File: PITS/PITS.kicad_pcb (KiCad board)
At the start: 2 copper layers, 65 x 30 mm, 56 parts, among them P1 CONN_02X20, P10 I2C, P11 I2C, P12 I2C, P13 I2C, P14 BATT, P2 BNC, P3 BNC, P4 BNC, P5 BNC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

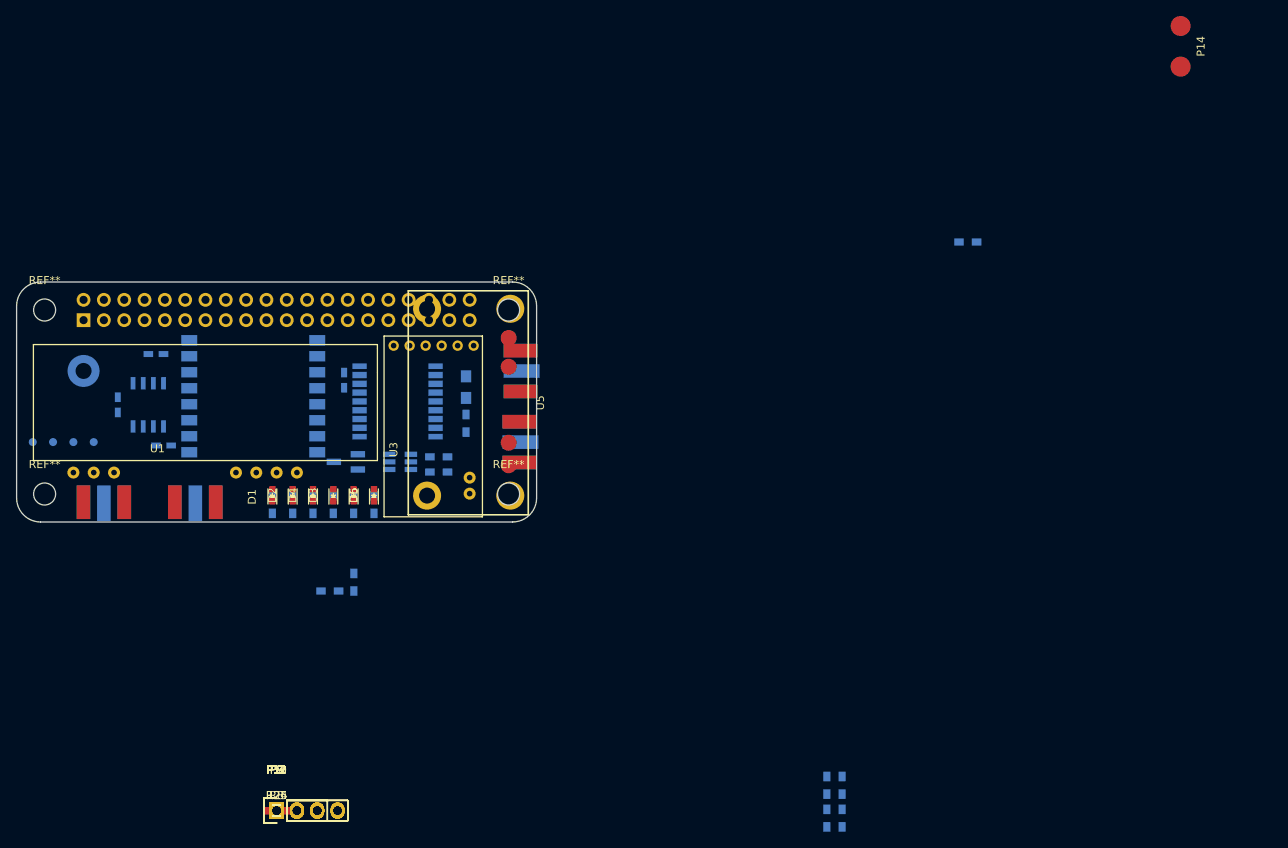
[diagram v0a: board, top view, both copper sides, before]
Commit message: layout - work in progress - first placement
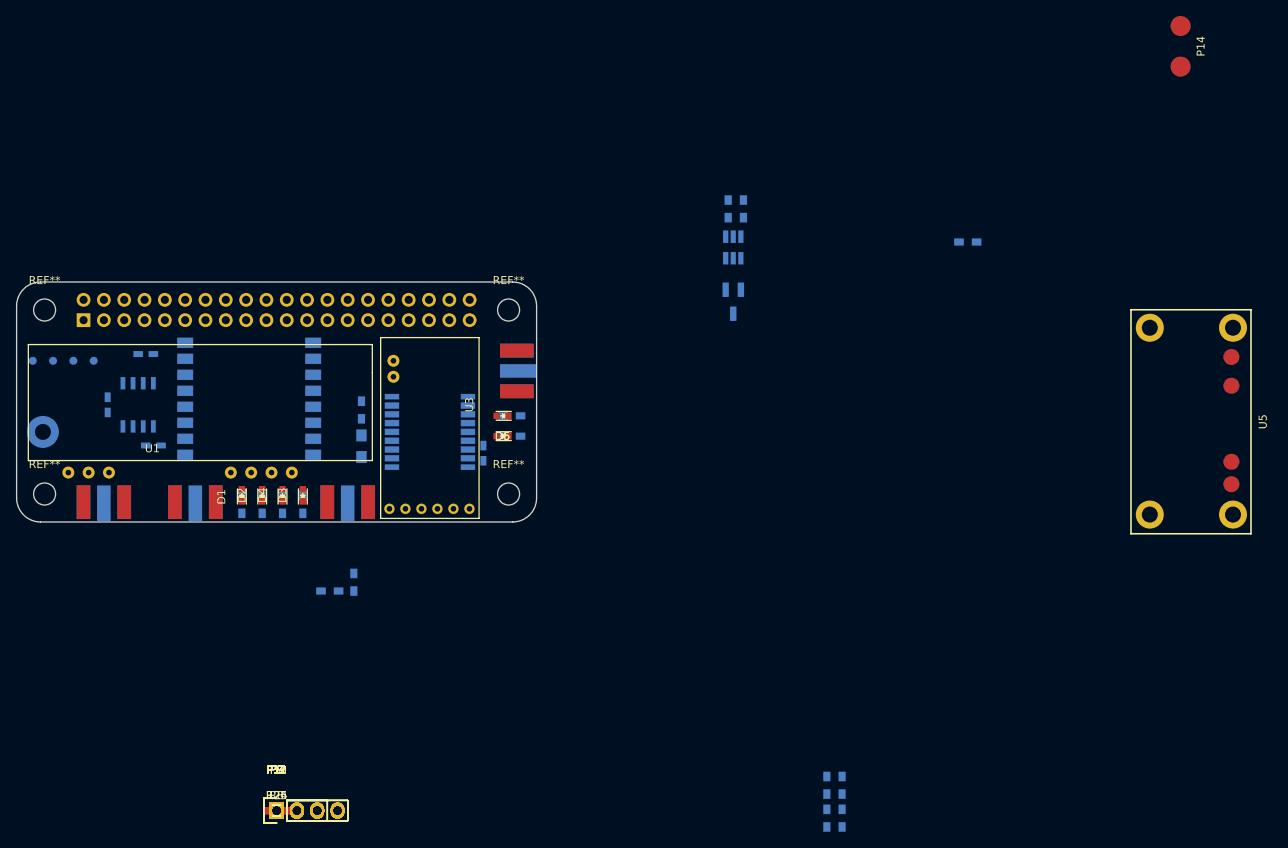
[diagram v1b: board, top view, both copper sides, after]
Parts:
- moved U5 90.4 mm to (201.8, 66.5)
- moved Q1 52.4 mm to (144.6, 51.5), turned to 0 degrees
- moved R19 50.3 mm to (145.9, 39.9), turned to 90 degrees
- moved Q2 49.5 mm to (144.6, 44.7), turned to 270 degrees
- moved R6 47.6 mm to (143.9, 39.9), turned to 90 degrees
- moved P2 27.3 mm to (96.4, 76.6), turned to 90 degrees
- moved R22 21.5 mm to (116.9, 68.3), turned to 180 degrees
- moved U3 20.5 mm to (101.6, 58.4), turned to 270 degrees
- moved R23 20.5 mm to (116.9, 65.7), turned to 180 degrees
- moved D5 20.0 mm to (115.7, 68.3), turned to 180 degrees
- moved C14 19.7 mm to (113.3, 70.4), turned to 90 degrees
- moved D6 18.9 mm to (115.7, 65.7), turned to 180 degrees
- moved L1 15.0 mm to (98.1, 69.5), turned to 90 degrees
- moved U2 14.4 mm to (111.4, 63.3), turned to 0 degrees
- moved R1 13.2 mm to (98.1, 65.0), turned to 270 degrees
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
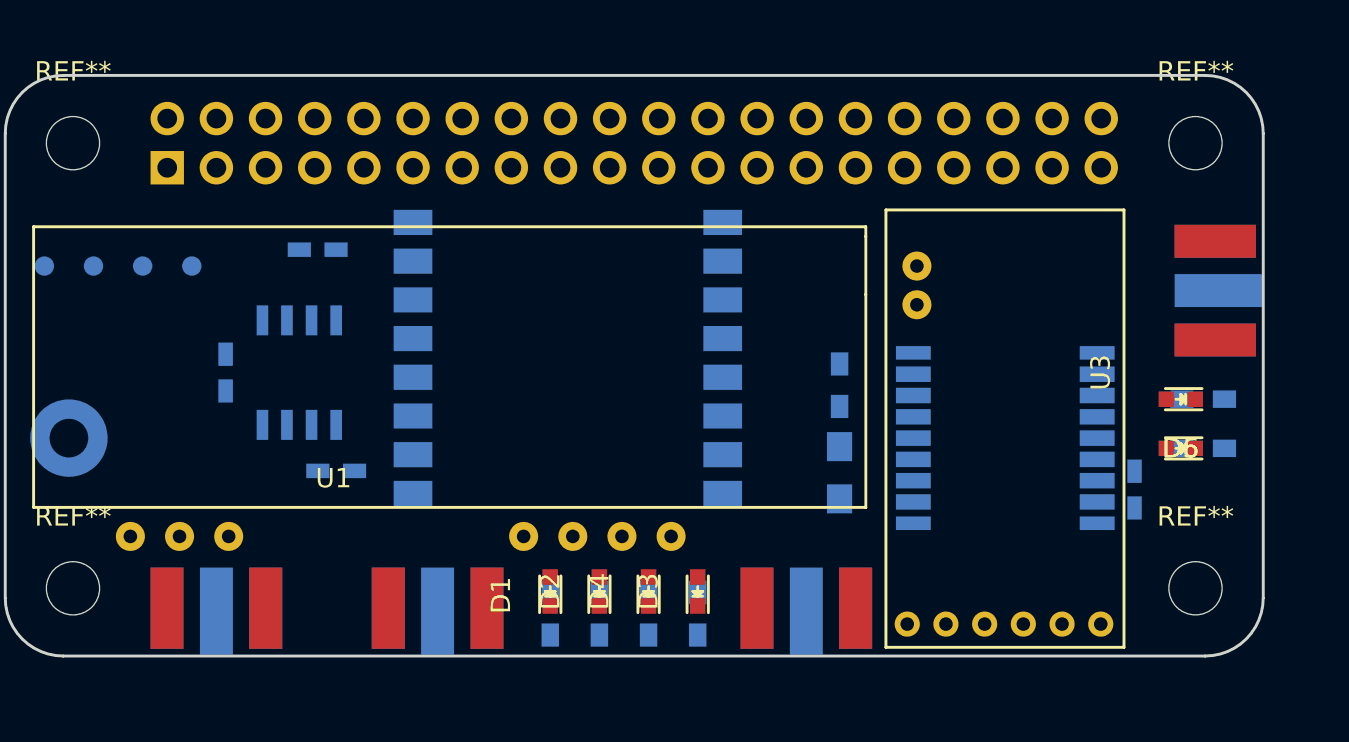
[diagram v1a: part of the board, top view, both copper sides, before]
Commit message: layout - work in progress - first placement
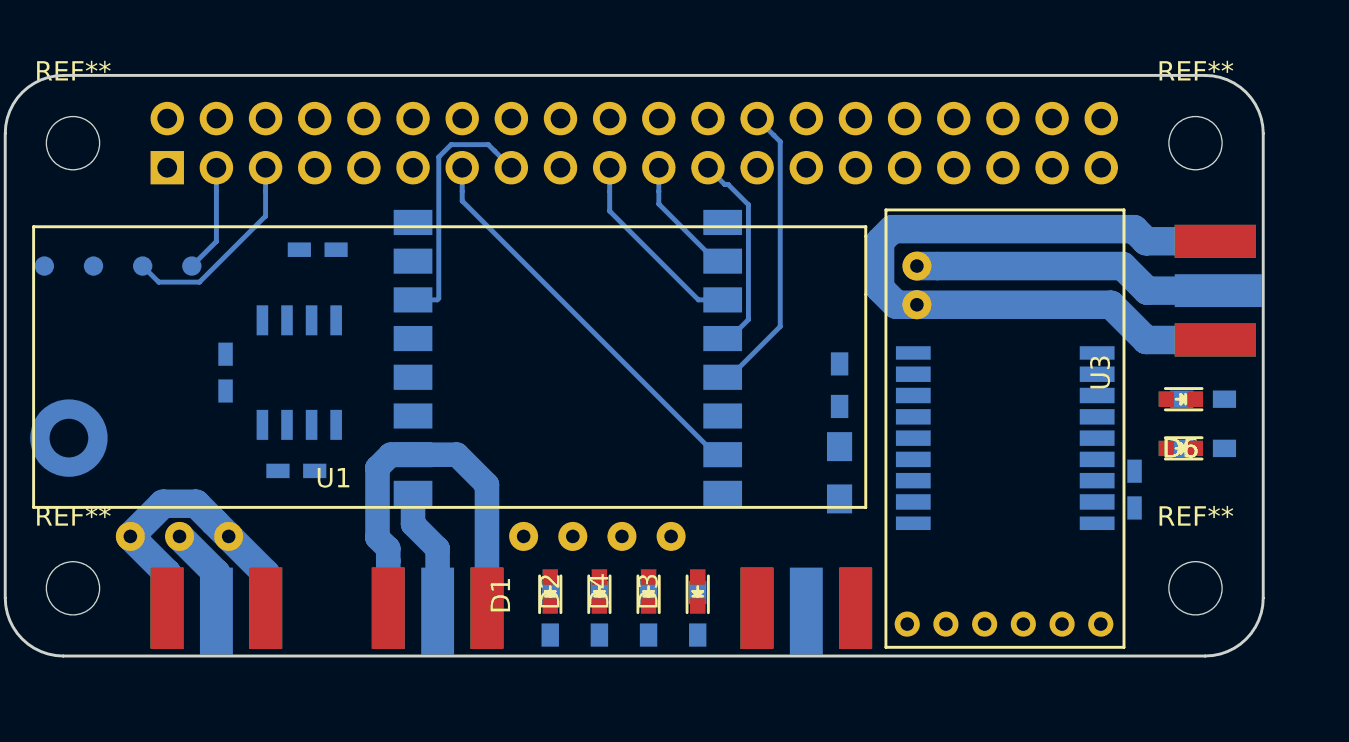
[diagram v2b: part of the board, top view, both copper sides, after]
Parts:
- moved C2 2.06 mm to (70.0, 69.4)
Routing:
- net GND: track 0.00 -> 74.6 mm
- net /GPIO27: track 0.00 -> 20.6 mm
- net Net-(P4-Pad1): track 0.00 -> 16.1 mm
- net /GPIO7(CE1): track 0.00 -> 15.3 mm
- net /GPIO22: track 0.00 -> 13.2 mm
- net /GPIO3(SCL1): track 0.00 -> 10.6 mm
- net /GPIO11(SCLK0): track 0.00 -> 10.6 mm
- net /GPIO10(MOSI0): track 0.00 -> 9.98 mm
- net Net-(P5-Pad1): track 0.00 -> 6.61 mm
- net /GPIO9(MISO0): track 0.00 -> 6.40 mm
- net /GPIO2(SDA1): track 0.00 -> 5.61 mm
- net Net-(P3-Pad1): track 0.00 -> 4.65 mm
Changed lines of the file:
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@@
     (thickness 1.6)
     (drawings 10)
-    (tracks 0)
+    (tracks 74)
     (zones 0)
     (modules 56)
@@
   )
   (setup
-    (last_trace_width 0.9144)
+    (last_trace_width 0.254)
     (user_trace_width 0.4064)
     (user_trace_width 0.9144)
@@
   )
   (module Capacitors_SMD:C_0603_HandSoldering (layer B.Cu)
-    (at 72.1 69.435 180)
+    (at 70.04 69.435 180)
     (descr "Capacitor SMD 0603, hand soldering")
     (tags "capacitor 0603")
@@
   (gr_arc (start 58 52) (end 55 52) (angle 90) (layer Edge.Cuts) (width 0.15))
   (gr_line (start 58 79) (end 117 79) (angle 90) (layer Edge.Cuts) (width 0.15))
+  (segment (start 65.91 54.991314) (end 65.91 53.77) (width 0.254) (layer B.Cu) (net 3))
+  (segment (start 65.91 57.58) (end 65.91 54.991314) (width 0.254) (layer B.Cu) (net 3))
+  (segment (start 64.64 58.85) (end 65.91 57.58) (width 0.254) (layer B.Cu) (net 3))
+  (segment (start 65.038497 59.680201) (end 68.45 56.268698) (width 0.254) (layer B.Cu) (net 4))
+  (segment (start 62.930201 59.680201) (end 65.038497 59.680201) (width 0.254) (layer B.Cu) (net 4))
+  (segment (start 68.45 54.991314) (end 68.45 53.77) (width 0.254) (layer B.Cu) (net 4))
+  (segment (start 62.1 58.85) (end 62.930201 59.680201) (width 0.254) (layer B.Cu) (net 4))
+  (segment (start 68.45 56.268698) (end 68.45 54.991314) (width 0.254) (layer B.Cu) (net 4))
+  (segment (start 117.5244 57.57) (end 113.9512 57.57) (width 1.4732) (layer B.Cu) (net 5))
+  (segment (start 113.9512 57.57) (end 113.3262 56.945) (width 1.4732) (layer B.Cu) (net 5))
+  (segment (start 113.3262 56.945) (end 100.835 56.945) (width 1.4732) (layer B.Cu) (net 5))
+  (segment (start 100.835 56.945) (end 100.2 57.58) (width 1.4732) (layer B.Cu) (net 5))
+  (segment (start 100.2 57.58) (end 100.2 60.00566) (width 1.4732) (layer B.Cu) (net 5))
+  (segment (start 100.2 60.00566) (end 101.04434 60.85) (width 1.4732) (layer B.Cu) (net 5))
+  (segment (start 101.04434 60.85) (end 102.105 60.85) (width 1.4732) (layer B.Cu) (net 5))
+  (segment (start 102.105 60.85) (end 112.1312 60.85) (width 1.4732) (layer B.Cu) (net 5))
+  (segment (start 117.5244 62.67) (end 113.9512 62.67) (width 1.4732) (layer B.Cu) (net 5))
+  (segment (start 113.9512 62.67) (end 112.1312 60.85) (width 1.4732) (layer B.Cu) (net 5))
+  (segment (start 76.07 68.5975) (end 74.911238 68.5975) (width 1.27) (layer B.Cu) (net 5))
+  (segment (start 74.911238 68.5975) (end 74.231799 69.276939) (width 1.27) (layer B.Cu) (net 5))
+  (segment (start 74.231799 69.276939) (end 74.231799 72.886799) (width 1.27) (layer B.Cu) (net 5))
+  (segment (start 74.79 73.445) (end 74.79 74.08) (width 1.27) (layer B.Cu) (net 5))
+  (segment (start 74.231799 72.886799) (end 74.79 73.445) (width 1.27) (layer B.Cu) (net 5))
+  (segment (start 74.79 74.08) (end 74.79 76.53) (width 1.27) (layer B.Cu) (net 5))
+  (segment (start 79.89 76.53) (end 79.89 70.1475) (width 1.27) (layer B.Cu) (net 5))
+  (segment (start 79.89 70.1475) (end 78.34 68.5975) (width 1.27) (layer B.Cu) (net 5))
+  (segment (start 78.34 68.5975) (end 76.07 68.5975) (width 1.27) (layer B.Cu) (net 5))
+  (segment (start 61.465 72.82) (end 63.154801 71.130199) (width 1.4732) (layer B.Cu) (net 5))
+  (segment (start 63.154801 71.130199) (end 64.855199 71.130199) (width 1.4732) (layer B.Cu) (net 5))
+  (segment (start 64.855199 71.130199) (end 65.795001 72.070001) (width 1.4732) (layer B.Cu) (net 5))
+  (segment (start 65.795001 72.070001) (end 66.545 72.82) (width 1.4732) (layer B.Cu) (net 5))
+  (segment (start 63.36 76.53) (end 63.36 74.715) (width 1.4732) (layer B.Cu) (net 5))
+  (segment (start 63.36 74.715) (end 61.465 72.82) (width 1.4732) (layer B.Cu) (net 5))
+  (segment (start 68.46 76.53) (end 68.46 74.735) (width 1.4732) (layer B.Cu) (net 5))
+  (segment (start 68.46 74.735) (end 66.545 72.82) (width 1.4732) (layer B.Cu) (net 5))
+  (segment (start 92.07 68.5975) (end 91.72 68.5975) (width 0.254) (layer B.Cu) (net 11))
+  (segment (start 91.72 68.5975) (end 78.61 55.4875) (width 0.254) (layer B.Cu) (net 11))
+  (segment (start 78.61 55.4875) (end 78.61 54.991314) (width 0.254) (layer B.Cu) (net 11))
+  (segment (start 78.61 54.991314) (end 78.61 53.77) (width 0.254) (layer B.Cu) (net 11))
+  (segment (start 76.07 60.5975) (end 77.324 60.5975) (width 0.254) (layer B.Cu) (net 12))
+  (segment (start 77.400201 60.521299) (end 77.400201 53.212973) (width 0.254) (layer B.Cu) (net 12))
+  (segment (start 77.324 60.5975) (end 77.400201 60.521299) (width 0.254) (layer B.Cu) (net 12))
+  (segment (start 77.400201 53.212973) (end 78.036975 52.576199) (width 0.254) (layer B.Cu) (net 12))
+  (segment (start 78.036975 52.576199) (end 79.956199 52.576199) (width 0.254) (layer B.Cu) (net 12))
+  (segment (start 79.956199 52.576199) (end 80.286401 52.906401) (width 0.254) (layer B.Cu) (net 12))
+  (segment (start 80.286401 52.906401) (end 81.15 53.77) (width 0.254) (layer B.Cu) (net 12))
+  (segment (start 92.07 60.5975) (end 90.816 60.5975) (width 0.254) (layer B.Cu) (net 13))
+  (segment (start 90.816 60.5975) (end 86.23 56.0115) (width 0.254) (layer B.Cu) (net 13))
+  (segment (start 86.23 54.991314) (end 86.23 53.77) (width 0.254) (layer B.Cu) (net 13))
+  (segment (start 86.23 56.0115) (end 86.23 54.991314) (width 0.254) (layer B.Cu) (net 13))
+  (segment (start 92.07 58.5975) (end 91.72 58.5975) (width 0.254) (layer B.Cu) (net 14))
+  (segment (start 91.72 58.5975) (end 88.77 55.6475) (width 0.254) (layer B.Cu) (net 14))
+  (segment (start 88.77 55.6475) (end 88.77 54.991314) (width 0.254) (layer B.Cu) (net 14))
+  (segment (start 88.77 54.991314) (end 88.77 53.77) (width 0.254) (layer B.Cu) (net 14))
+  (segment (start 92.07 62.5975) (end 92.42 62.5975) (width 0.254) (layer B.Cu) (net 16))
+  (segment (start 92.42 62.5975) (end 93.400201 61.617299) (width 0.254) (layer B.Cu) (net 16))
+  (segment (start 93.400201 61.617299) (end 93.400201 55.683339) (width 0.254) (layer B.Cu) (net 16))
+  (segment (start 92.350461 54.633599) (end 92.173599 54.633599) (width 0.254) (layer B.Cu) (net 16))
+  (segment (start 93.400201 55.683339) (end 92.350461 54.633599) (width 0.254) (layer B.Cu) (net 16))
+  (segment (start 92.173599 54.633599) (end 91.31 53.77) (width 0.254) (layer B.Cu) (net 16))
+  (segment (start 92.07 64.5975) (end 92.42 64.5975) (width 0.254) (layer B.Cu) (net 17))
+  (segment (start 92.42 64.5975) (end 95.043801 61.973699) (width 0.254) (layer B.Cu) (net 17))
+  (segment (start 95.043801 61.973699) (end 95.043801 52.423801) (width 0.254) (layer B.Cu) (net 17))
+  (segment (start 94.713599 52.093599) (end 93.85 51.23) (width 0.254) (layer B.Cu) (net 17))
+  (segment (start 95.043801 52.423801) (end 94.713599 52.093599) (width 0.254) (layer B.Cu) (net 17))
+  (segment (start 65.91 76.68) (end 65.91 74.725) (width 1.4732) (layer B.Cu) (net 33))
+  (segment (start 65.91 74.725) (end 64.005 72.82) (width 1.4732) (layer B.Cu) (net 33))
+  (segment (start 103.16566 58.85) (end 102.105 58.85) (width 1.4732) (layer B.Cu) (net 34))
+  (segment (start 112.730803 58.85) (end 103.16566 58.85) (width 1.4732) (layer B.Cu) (net 34))
+  (segment (start 114.000803 60.12) (end 112.730803 58.85) (width 1.4732) (layer B.Cu) (net 34))
+  (segment (start 117.6744 60.12) (end 114.000803 60.12) (width 1.4732) (layer B.Cu) (net 34))
+  (segment (start 77.34 76.68) (end 77.34 73.455) (width 1.27) (layer B.Cu) (net 35))
+  (segment (start 77.34 73.455) (end 76.07 72.185) (width 1.27) (layer B.Cu) (net 35))
+  (segment (start 76.07 72.185) (end 76.07 70.5975) (width 1.27) (layer B.Cu) (net 35))
 )
